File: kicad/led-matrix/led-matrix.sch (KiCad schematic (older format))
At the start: 4 parts

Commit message: Update schematix
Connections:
- net at U?.4 (DRAIN0): now also U?.13 (A0)
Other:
- moved on the sheet: U?
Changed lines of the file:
@@
 $EndDescr
-$Comp
-L Interface_Expansion:TPIC6595 U?
-U 1 1 5FD7CD50
-P 5150 3100
-F 0 "U?" H 5150 3881 50  0000 C CNN
-F 1 "TPIC6595" H 5150 3790 50  0000 C CNN
-F 2 "" H 5800 2450 50  0001 C CNN
-F 3 "http://www.ti.com/lit/ds/symlink/tpic6595.pdf" H 5150 3050 50  0001 C CNN
-	1    5150 3100
-	1    0    0    -1
-$EndComp
-$Comp
-L 74xx:74HCT4051 U?
-U 1 1 5FD7E6DB
-P 7400 2950
-F 0 "U?" H 7450 3631 50  0000 C CNN
-F 1 "74HCT4051" H 7450 3540 50  0000 C CNN
-F 2 "" H 7400 2550 50  0001 C CNN
-F 3 "http://www.ti.com/lit/ds/symlink/cd74hct4051.pdf" H 7400 2550 50  0001 C CNN
-	1    7400 2950
-	1    0    0    -1
-$EndComp
 $Comp
 L MIC2981:MIC2981_82YN U?
@@
 	1    0    0    -1
 $EndComp
+Wire Wire Line
+	7900 2600 8350 2600
+Wire Wire Line
+	8350 2600 8350 2650
+$Comp
+L 74xx:74HCT4051 U?
+U 1 1 5FD7E6DB
+P 8750 2950
+F 0 "U?" H 8800 3631 50  0000 C CNN
+F 1 "74HCT4051" H 8800 3540 50  0000 C CNN
+F 2 "" H 8750 2550 50  0001 C CNN
+F 3 "http://www.ti.com/lit/ds/symlink/cd74hct4051.pdf" H 8750 2550 50  0001 C CNN
+	1    8750 2950
+	-1   0    0    -1
+$EndComp
+$Comp
+L Interface_Expansion:TPIC6595 U?
+U 1 1 5FD7CD50
+P 7400 3000
+F 0 "U?" H 7400 3781 50  0000 C CNN
+F 1 "TPIC6595" H 7400 3690 50  0000 C CNN
+F 2 "" H 8050 2350 50  0001 C CNN
+F 3 "http://www.ti.com/lit/ds/symlink/tpic6595.pdf" H 7400 2950 50  0001 C CNN
+	1    7400 3000
+	1    0    0    -1
+$EndComp

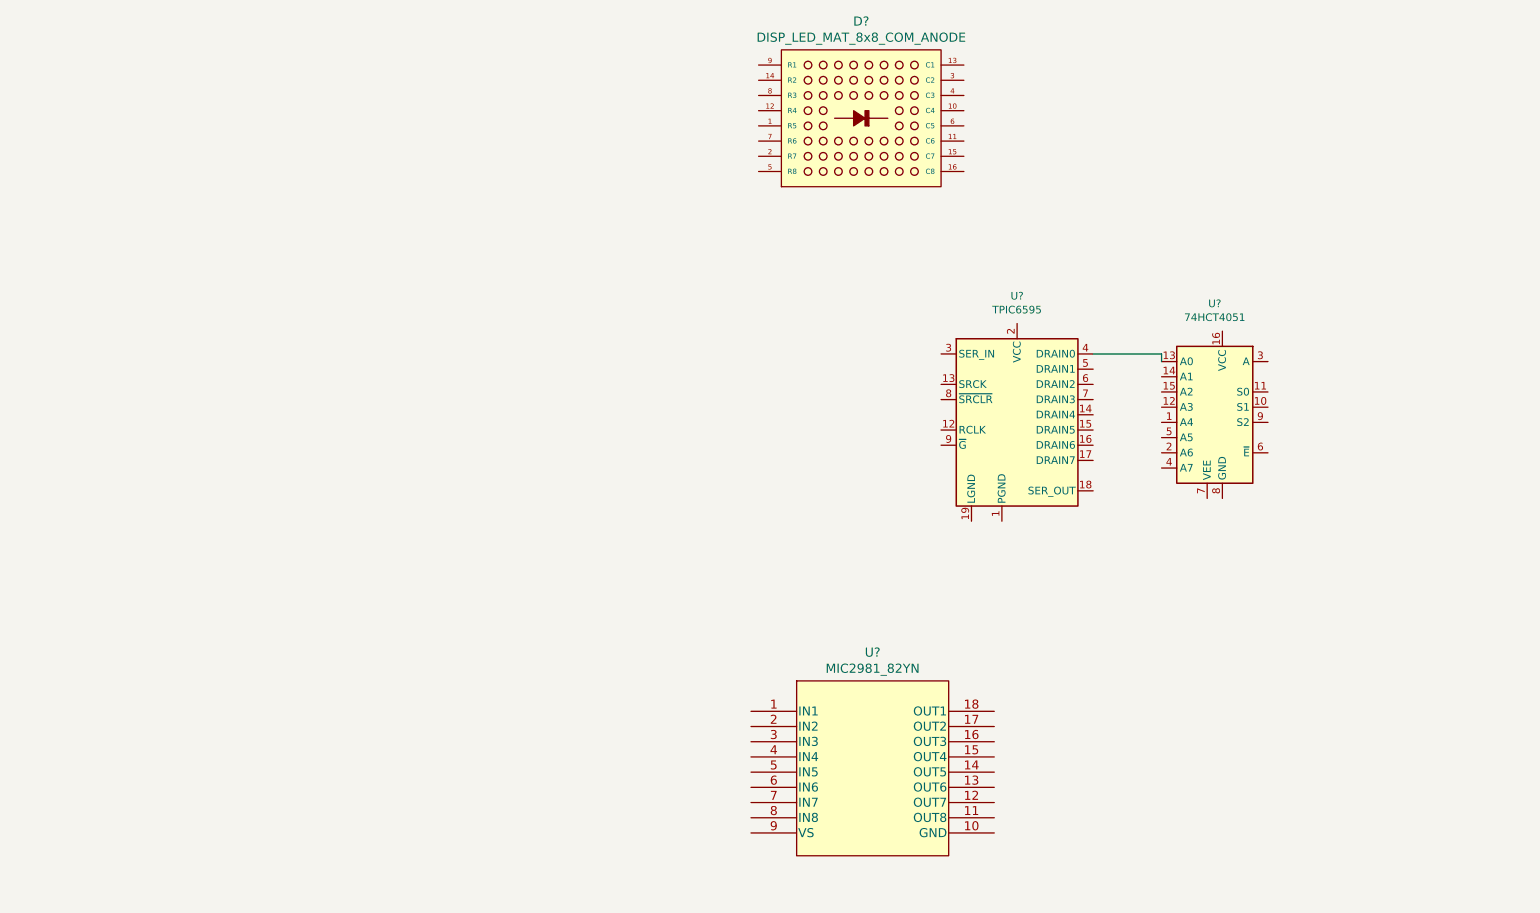
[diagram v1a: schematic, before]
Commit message: KiCad: Update schematic
Now contains main pipeline
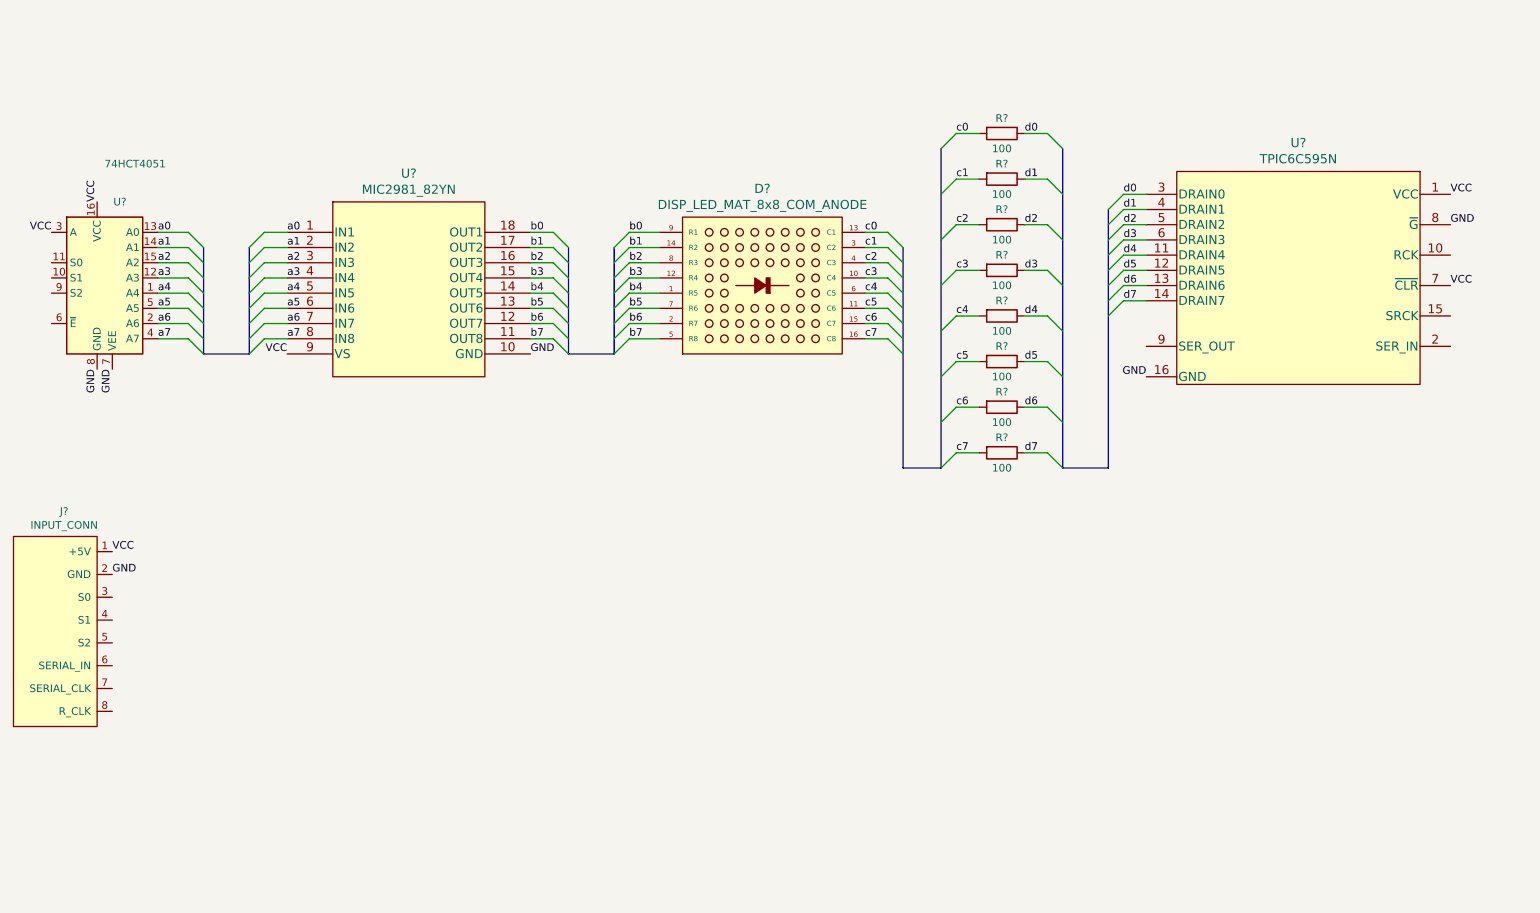
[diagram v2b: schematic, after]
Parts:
- removed U?: TPIC6595, symbol Interface_Expansion:TPIC6595
- added J?: INPUT_CONN, symbol myConnectors:INPUT_CONN
- added R? (x8): 100, symbol Device:R
- added U?: TPIC6C595N, N0016A, symbol TPIC6C595N:TPIC6C595N
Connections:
- net a0: now reaches U?.13 (A0)
- net a0: now also U?.1 (IN1)
- net a4: now reaches U?.1 (A4)
- net a4: now also U?.5 (IN5)
- net a3: now reaches U?.12 (A3)
- net a3: now also U?.4 (IN4)
- net a1: now reaches U?.14 (A1)
- net a1: now also U?.2 (IN2)
- net a2: now reaches U?.15 (A2)
- net a2: now also U?.3 (IN3)
- net VCC: now reaches U?.16 (VCC)
- net VCC: now also U?.3 (A), U?.9 (VS), J?.1 (+5V), U?.1 (VCC), U?.7 (~CLR)
- net a6: now reaches U?.2 (A6)
- net a6: now also U?.7 (IN7)
- net a7: now reaches U?.4 (A7)
- net a7: now also U?.8 (IN8)
- net a5: now reaches U?.5 (A5)
- net a5: now also U?.6 (IN6)
- net GND: now reaches U?.7 (VEE)
- net GND: now also U?.10 (GND), U?.8 (GND), J?.2 (GND), U?.16 (GND), U?.8 (~G)
- net b7: now reaches U?.11 (OUT8)
- net b7: now also D?.5 (R8)
- net b6: now reaches U?.12 (OUT7)
- net b6: now also D?.2 (R7)
- net b5: now reaches U?.13 (OUT6)
- net b5: now also D?.7 (R6)
- net b4: now reaches U?.14 (OUT5)
- net b4: now also D?.1 (R5)
- net b3: now reaches U?.15 (OUT4)
- net b3: now also D?.12 (R4)
- net b2: now reaches U?.16 (OUT3)
- net b2: now also D?.8 (R3)
- net b1: now reaches U?.17 (OUT2)
- net b1: now also D?.14 (R2)
- net b0: now reaches U?.18 (OUT1)
- net b0: now also D?.9 (R1)
- net c3: now reaches D?.10 (C4)
- net c3: now also R?.2
- net c5: now reaches D?.11 (C6)
- net c5: now also R?.2
- net c0: now reaches D?.13 (C1)
- net c0: now also R?.2
- net c6: now reaches D?.15 (C7)
- net c6: now also R?.2
- net c7: now reaches D?.16 (C8)
- net c7: now also R?.2
- net c1: now reaches D?.3 (C2)
- net c1: now also R?.2
- net c2: now reaches D?.4 (C3)
- net c2: now also R?.2
- net c4: now reaches D?.6 (C5)
- net c4: now also R?.2
- new net d0: R?.1, U?.3 (DRAIN0)
- new net d1: R?.1, U?.4 (DRAIN1)
- new net d2: R?.1, U?.5 (DRAIN2)
- new net d3: R?.1, U?.6 (DRAIN3)
- new net d4: R?.1, U?.11 (DRAIN4)
- new net d5: R?.1, U?.12 (DRAIN5)
- new net d6: R?.1, U?.13 (DRAIN6)
- new net d7: R?.1, U?.14 (DRAIN7)
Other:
- moved on the sheet: D?, U?

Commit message: KiCad: Finish labeling as far as possible
Still need to add an output header
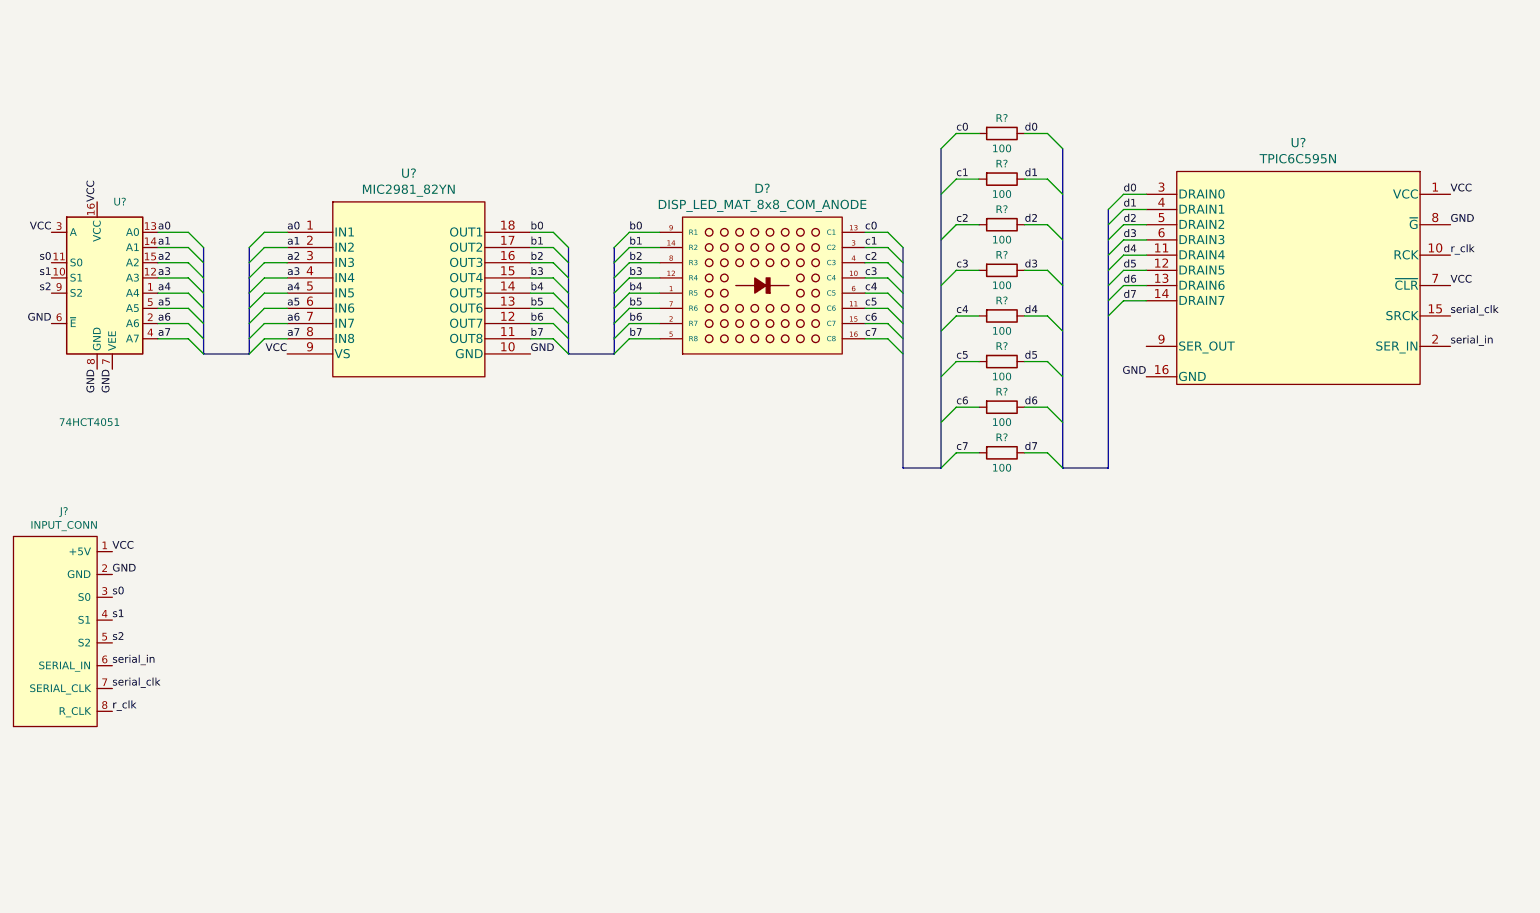
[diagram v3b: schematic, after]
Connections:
- net GND: now also U?.6 (~E)
- net s1: now reaches U?.10 (S1)
- net s1: now also J?.4 (S1)
- net s0: now reaches U?.11 (S0)
- net s0: now also J?.3 (S0)
- net s2: now reaches U?.9 (S2)
- net s2: now also J?.5 (S2)
- net serial_in: now reaches J?.6 (SERIAL_IN)
- net serial_in: now also U?.2 (SER_IN)
- net serial_clk: now reaches J?.7 (SERIAL_CLK)
- net serial_clk: now also U?.15 (SRCK)
- net r_clk: now reaches J?.8 (R_CLK)
- net r_clk: now also U?.10 (RCK)
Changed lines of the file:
@@
 P 1350 2100
 F 0 "U?" H 1500 2600 50  0000 C CNN
-F 1 "74HCT4051" H 1600 2850 50  0000 C CNN
+F 1 "74HCT4051" H 1300 1150 50  0000 C CNN
 F 2 "" H 1350 1700 50  0001 C CNN
 F 3 "http://www.ti.com/lit/ds/symlink/cd74hct4051.pdf" H 1350 1700 50  0001 C CNN
 	1    1350 2100
-	1    0    0    -1
-$EndComp
-$Comp
-L myConnectors:INPUT_CONN J?
-U 1 1 5FDA3D76
-P 1450 3750
-F 0 "J?" H 1133 3865 50  0000 C CNN
-F 1 "INPUT_CONN" H 1133 3774 50  0000 C CNN
-F 2 "" H 1450 3750 50  0001 C CNN
-F 3 "" H 1450 3750 50  0001 C CNN
-	1    1450 3750
 	1    0    0    -1
 $EndComp
@@
 Wire Bus Line
 	7700 3350 8000 3350
+Text Label 1050 2400 2    50   ~ 0
+GND
+Text Label 1450 4200 0    50   ~ 0
+s0
+Text Label 1050 2000 2    50   ~ 0
+s0
+Text Label 1450 4350 0    50   ~ 0
+s1
+Text Label 1450 4500 0    50   ~ 0
+s2
+Text Label 1050 2100 2    50   ~ 0
+s1
+Text Label 1050 2200 2    50   ~ 0
+s2
+Text Label 1450 4950 0    50   ~ 0
+r_clk
+Text Label 10250 1950 0    50   ~ 0
+r_clk
+Text Label 1450 4650 0    50   ~ 0
+serial_in
+Text Label 10250 2550 0    50   ~ 0
+serial_in
+Wire Bus Line
+	8000 1650 8000 3350
+Wire Bus Line
+	7700 1250 7700 3350
+Wire Bus Line
+	6900 1250 6900 3350
+Wire Bus Line
+	6650 1900 6650 3350
+Wire Bus Line
+	2050 1900 2050 2600
+Wire Bus Line
+	2350 1900 2350 2600
+Wire Bus Line
+	4450 1900 4450 2600
 Wire Bus Line
 	4750 1900 4750 2600
-Wire Bus Line
-	4450 1900 4450 2600
-Wire Bus Line
-	2350 1900 2350 2600
-Wire Bus Line
-	2050 1900 2050 2600
-Wire Bus Line
-	6900 1250 6900 3350
-Wire Bus Line
-	7700 1250 7700 3350
-Wire Bus Line
-	8000 1650 8000 3350
-Wire Bus Line
-	6650 1900 6650 3350
+$Comp
+L myConnectors:INPUT_CONN J?
+U 1 1 5FDA3D76
+P 1450 3750
+F 0 "J?" H 1133 3865 50  0000 C CNN
+F 1 "INPUT_CONN" H 1133 3774 50  0000 C CNN
+F 2 "" H 1450 3750 50  0001 C CNN
+F 3 "" H 1450 3750 50  0001 C CNN
+	1    1450 3750
+	1    0    0    -1
+$EndComp
+Text Label 1450 4800 0    50   ~ 0
+serial_clk
+Text Label 10250 2350 0    50   ~ 0
+serial_clk
 $EndSCHEMATC
